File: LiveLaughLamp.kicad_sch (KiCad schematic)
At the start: 16 parts, among them J1 SM04B-SRSS-TB, J2 SM04B-SRSS-TB, Q1 BSS138, SW1 1437566-3, U1 XIAO-ESP32-C3-SMD, U2 PCA9685BS, U3 PCA9306D

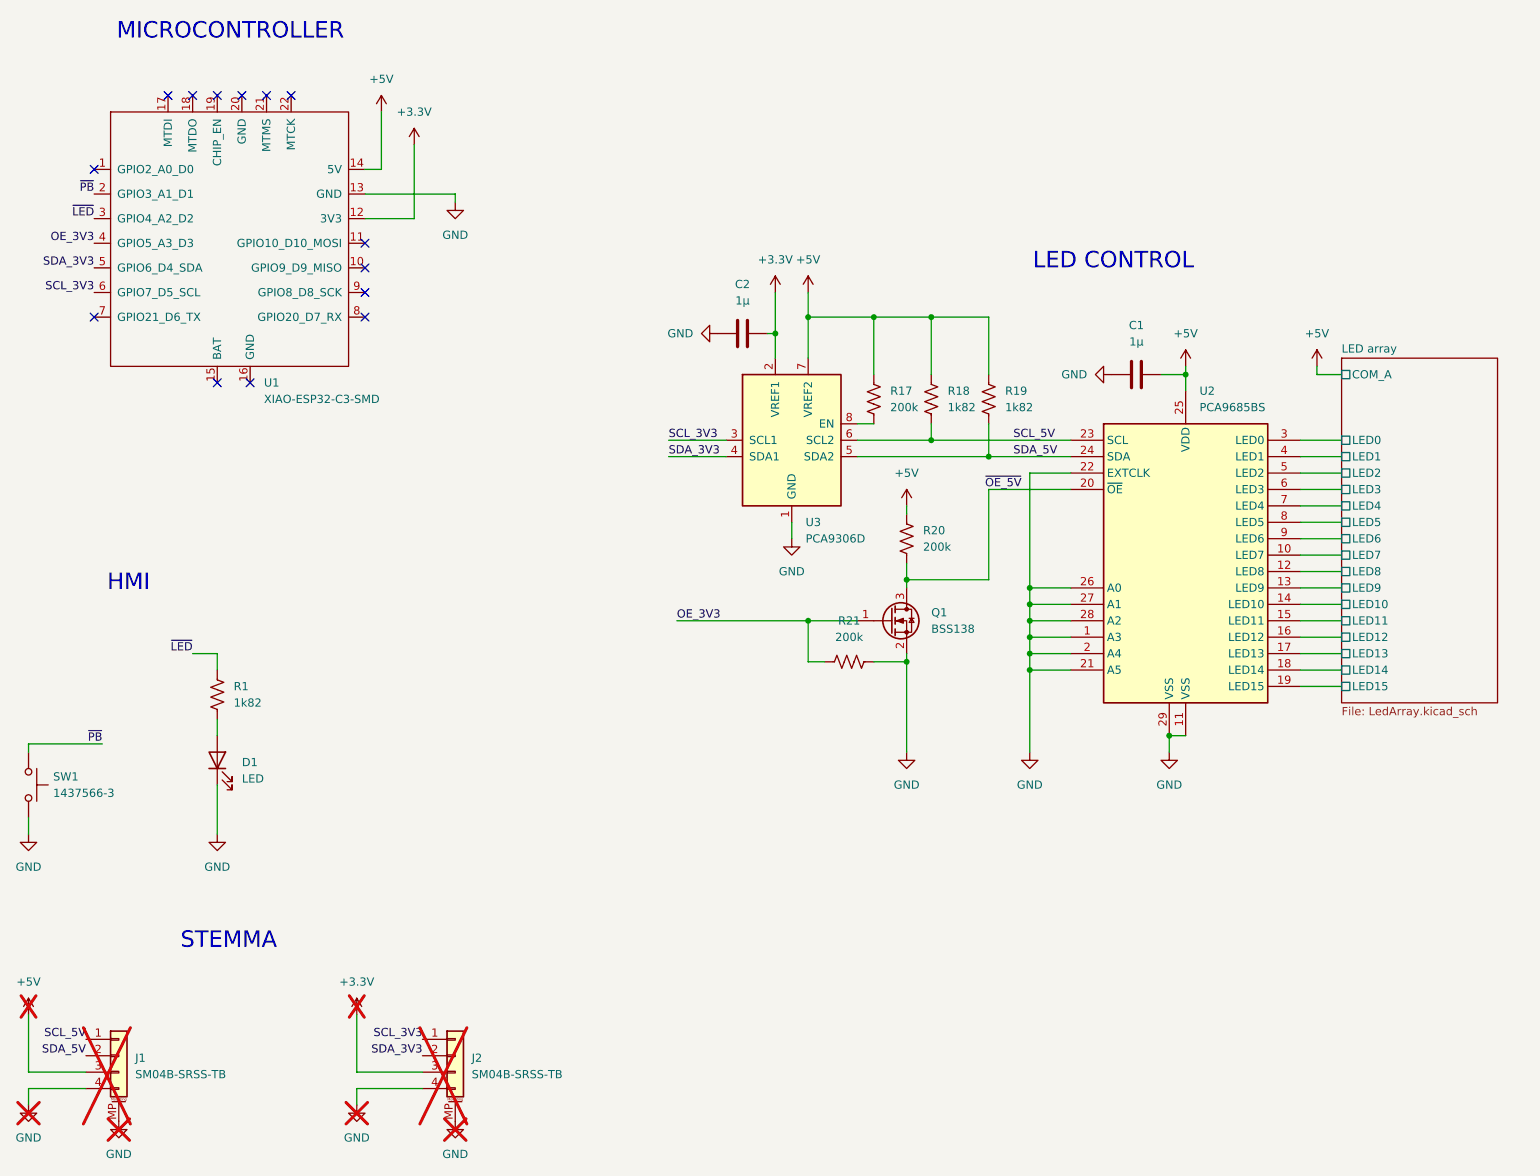
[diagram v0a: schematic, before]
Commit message: Swap LED controller for TLC5971
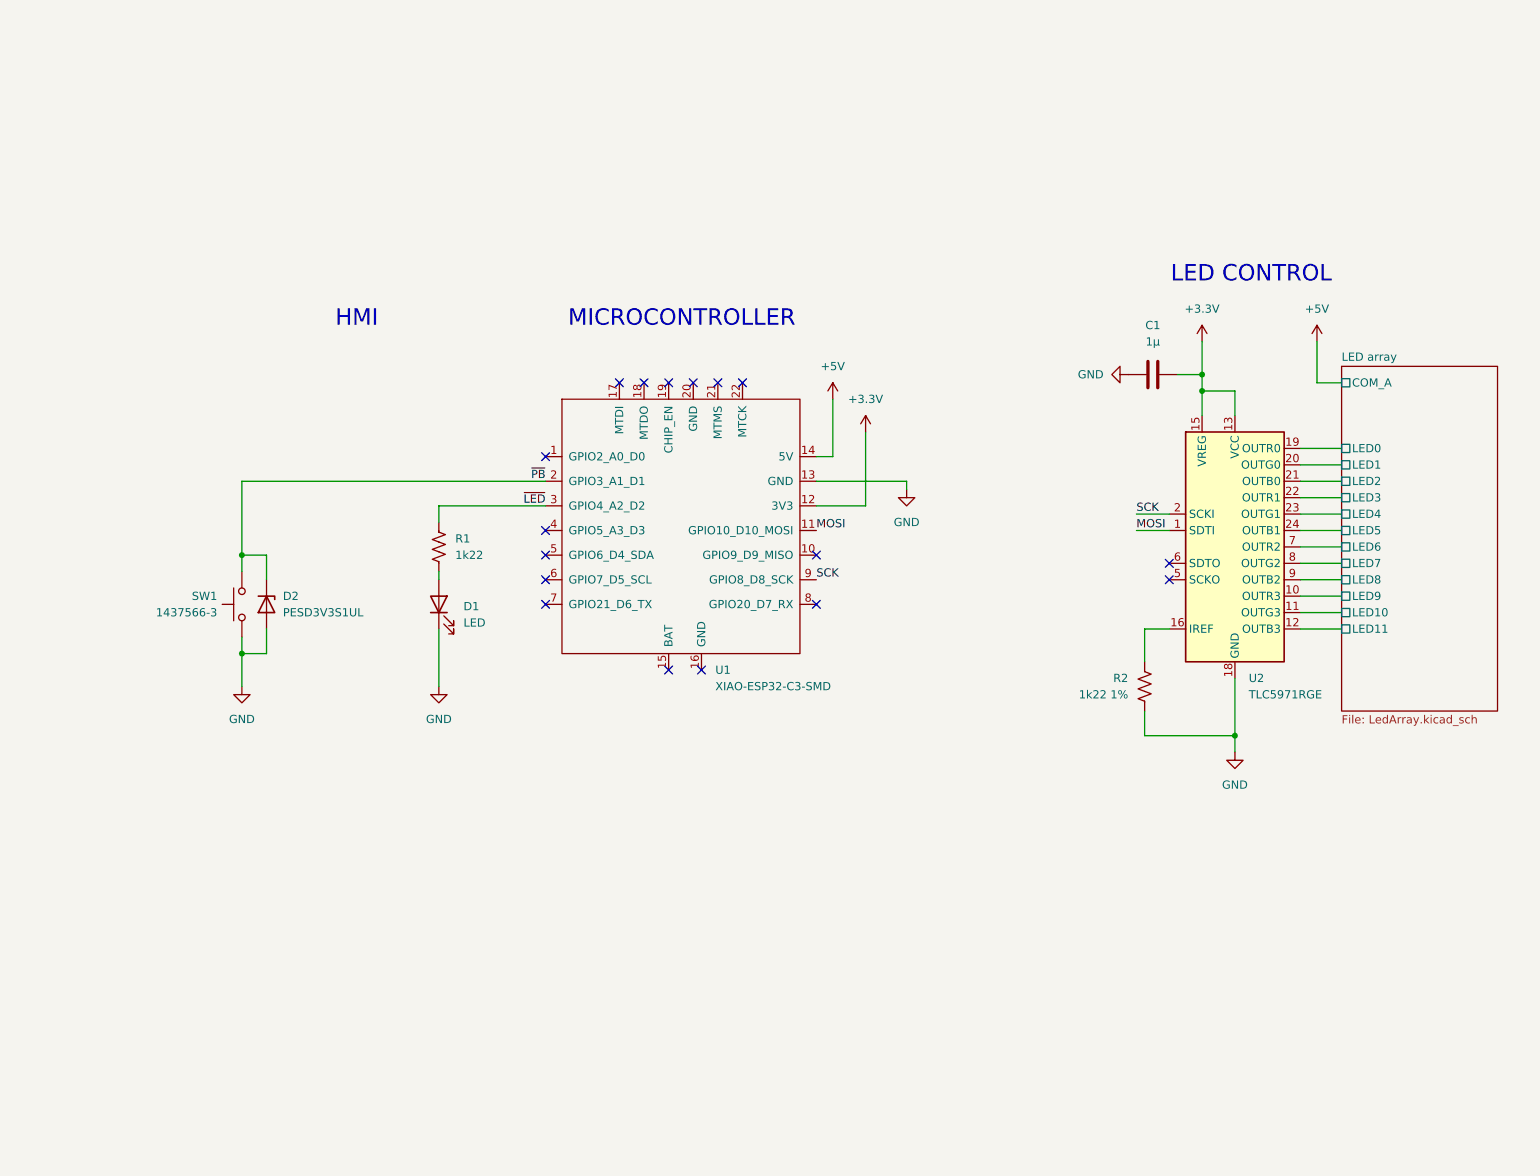
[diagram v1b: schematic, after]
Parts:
- removed C2: 1µ, Capacitor_SMD:C_0402_1005Metric, symbol Device:C
- removed J1, J2: SM04B-SRSS-TB, Connector_JST:JST_SH_SM04B-SRSS-TB_1x04-1MP_P1.00mm_Horizontal, symbol Connector_Generic_MountingPin:Conn_01x04_MountingPin
- removed Q1: BSS138, Package_TO_SOT_SMD:SOT-23, symbol Transistor_FET:BSS138
- removed R17, R20, R21: 200k, Resistor_SMD:R_0402_1005Metric, symbol Device:R_US
- removed R18, R19: 1k82, Resistor_SMD:R_0402_1005Metric, symbol Device:R_US
- removed U2: PCA9685BS, Package_DFN_QFN:QFN-28-1EP_6x6mm_P0.65mm_EP4.25x4.25mm, symbol Driver_LED:PCA9685BS
- removed U3: PCA9306D, Package_SO:VSSOP-8_2.3x2mm_P0.5mm, symbol Interface:PCA9306DC1
- added D2: PESD3V3S1UL, Diode_SMD:D_SOD-882, symbol Diode:PESD3V3S1UL
- added R2: 1k22 1%, Resistor_SMD:R_0402_1005Metric, symbol Device:R_US
- added U2: TLC5971RGE, Package_DFN_QFN:Texas_RGE0024H_VQFN-24-1EP_4x4mm_P0.5mm_EP2.7x2.7mm_ThermalVias, symbol Driver_LED:TLC5971RGE
- R1: value 1k82 -> 1k22
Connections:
- net +3.3V: now also C1.2, U2.13 (VCC), U2.15 (VREG)
- net +5V: no longer C1.2
- net GND: now also D2.2 (A), R2.2, U2.18 (GND), U2.25 (GND)
- net LED array/LED0: now also U2.19 (OUTR0)
- net LED array/LED1: now also U2.20 (OUTG0)
- net LED array/LED10: now also U2.11 (OUTG3)
- net LED array/LED11: now also U2.12 (OUTB3)
- net LED array/LED2: now also U2.21 (OUTB0)
- net LED array/LED3: now also U2.22 (OUTR1)
- net LED array/LED4: now also U2.23 (OUTG1)
- net LED array/LED5: now also U2.24 (OUTB1)
- net LED array/LED6: now also U2.7 (OUTR2)
- net LED array/LED7: now also U2.8 (OUTG2)
- net LED array/LED8: now also U2.9 (OUTB2)
- net LED array/LED9: now also U2.10 (OUTR3)
- net ~{PB}: now also D2.1 (K)
- net MOSI: now reaches U1.11 (GPIO10_D10_MOSI)
- net MOSI: now also U2.1 (SDTI)
- net SCK: now reaches U1.9 (GPIO8_D8_SCK)
- net SCK: now also U2.2 (SCKI)
- net OE_3V3: no longer names the net of U1.4 (GPIO5_A3_D3)
- net SCL_3V3: no longer names the net of U1.6 (GPIO7_D5_SCL)
- net SDA_3V3: no longer names the net of U1.5 (GPIO6_D4_SDA)
- new net: R2.1, U2.16 (IREF)
- no-connect marks 14 -> 17
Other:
- sheet LED array ports: added none; removed LED12, LED13, LED14, LED15
- note removed: "STEMMA"
- moved on the sheet: C1, D1, R1, SW1, U1

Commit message: Add thermal sink for Xiao board. Add JLC fabrication metadata.
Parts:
- added C2, C3: 22µ, Capacitor_SMD:C_0805_2012Metric, symbol Device:C
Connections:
- net +5V: now also C2.1, C3.1
- net GND: now also C2.2, C3.2

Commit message: Change some component values for better sourcing
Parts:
- D2: value PESD3V3S1UL -> PESD3V3L1ULSYL
- R1: value 1k22 -> 1k2 1%
- R2: value 1k22 1% -> 1k2 1%
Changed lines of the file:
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@@
 			)
 		)
-		(property "Value" "1k22"
+		(property "Value" "1k2 1%"
 			(at 91.44 106.6799 0)
 			(effects
@@
 			)
 		)
-		(property "Value" "1k22 1%"
+		(property "Value" "1k2 1%"
 			(at 195.58 128.2699 0)
 			(effects
@@
 			)
 		)
-		(property "Value" "PESD3V3S1UL"
+		(property "Value" "PESD3V3L1ULSYL"
 			(at 64.77 115.5699 90)
 			(effects
